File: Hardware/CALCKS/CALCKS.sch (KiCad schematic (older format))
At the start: 2 parts

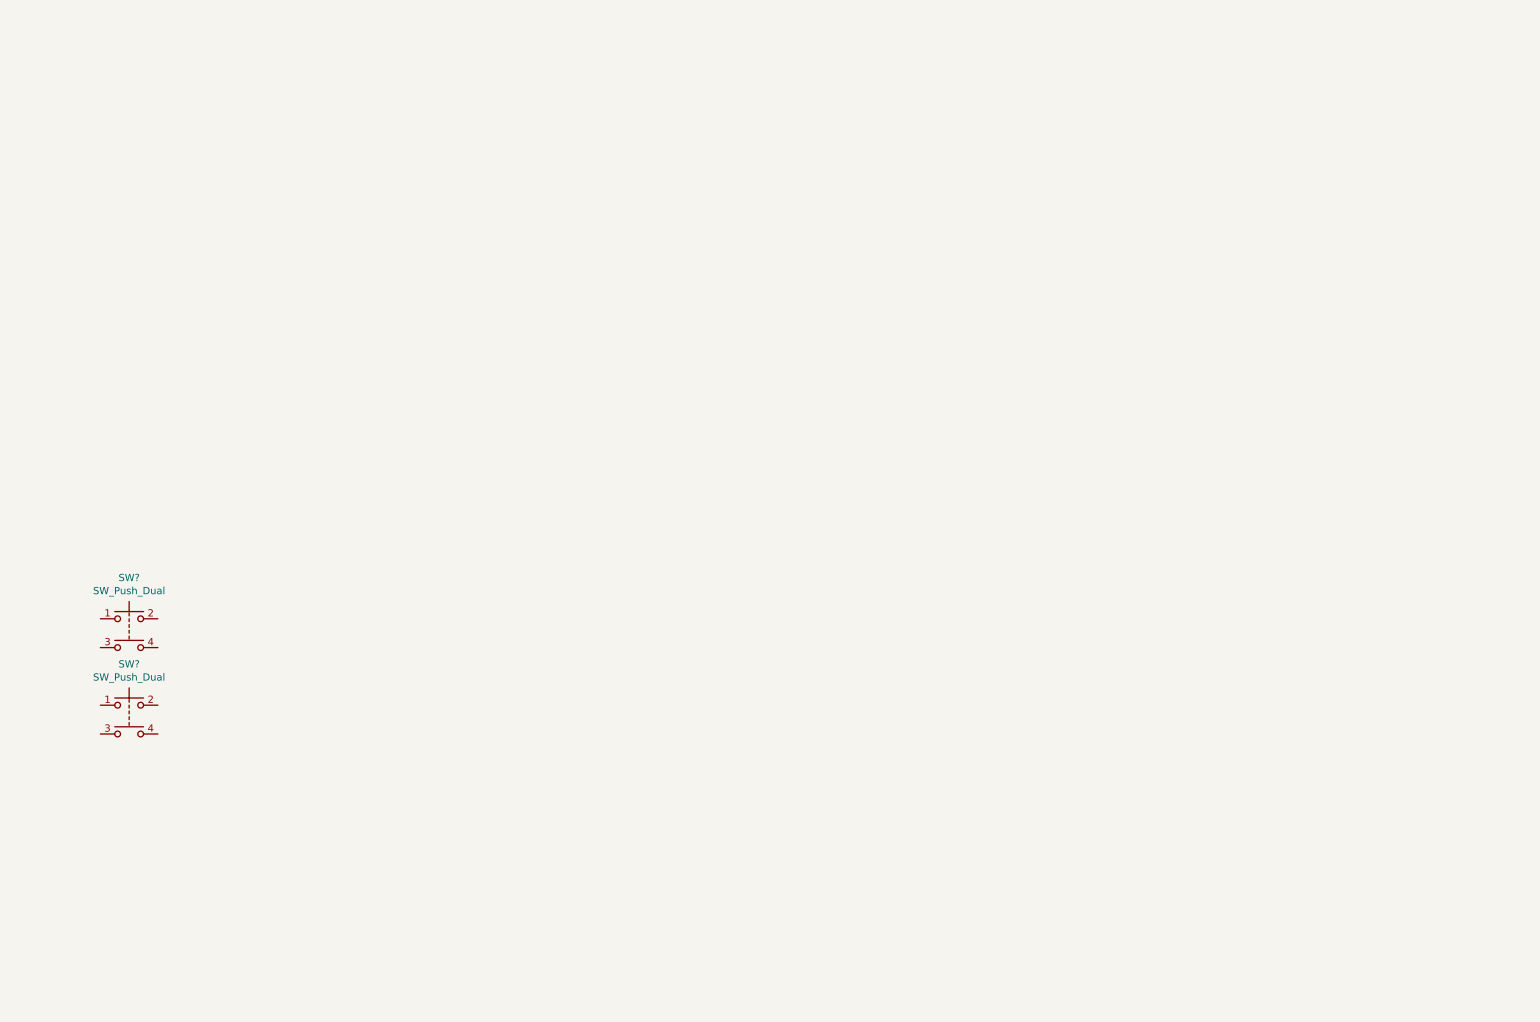
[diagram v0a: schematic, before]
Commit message: Add PCB progress from yesterday
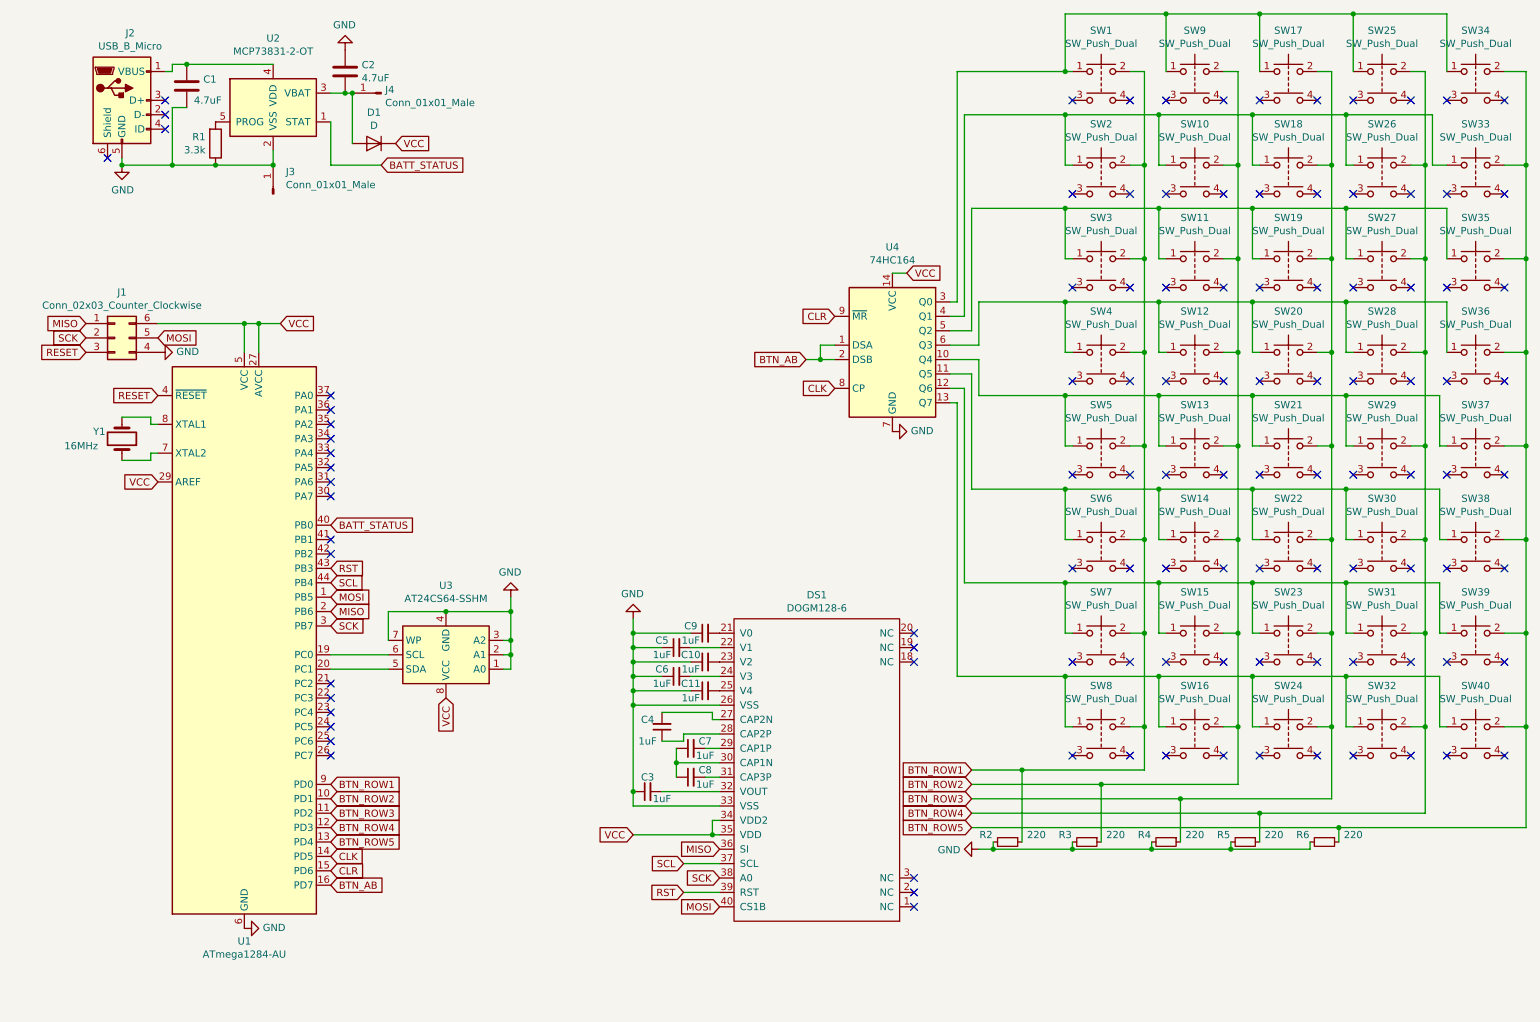
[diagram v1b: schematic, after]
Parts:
- removed SW? (x2): SW_Push_Dual, symbol Switch:SW_Push_Dual
- added C1, C2: 4.7uF, Capacitor_SMD:C_0805_2012Metric, symbol Device:C
- added C10, C11, C3, C4, C5, C6, C7, C8, C9: 1uF, Capacitor_SMD:C_0805_2012Metric, symbol Device:C_Small
- added D1: D, Diode_SMD:D_SOD-323, symbol Device:D
- added DS1: DOGM128-6, CALCKS:LCD_DOGM128-6, symbol Additional_Parts:DOGM128-6
- added J1: Conn_02x03_Counter_Clockwise, Connector_PinHeader_2.54mm:PinHeader_2x03_P2.54mm_Vertical, symbol Connector_Generic:Conn_02x03_Counter_Clockwise
- added J2: USB_B_Micro, Connector_USB:USB_Micro-B_Wuerth_629105150521, symbol Connector:USB_B_Micro
- added J3, J4: Conn_01x01_Male, TestPoint:TestPoint_Pad_D3.0mm, symbol Connector:Conn_01x01_Male
- added R1: 3.3k, Resistor_SMD:R_0805_2012Metric, symbol Device:R
- added R2, R3, R4, R5, R6: 220, Resistor_SMD:R_0805_2012Metric, symbol Device:R_Small
- added SW1, SW10, SW11, SW12, SW13, SW14, SW15, SW16, SW17, SW18, SW19, SW2, SW20, SW21, SW22, SW23, SW24, SW25, SW26, SW27, SW28, SW29, SW3, SW30, SW31, SW32, SW33, SW34, SW35, SW36, SW37, SW38, SW39, SW4, SW40, SW5, SW6, SW7, SW8, SW9: SW_Push_Dual, Downloaded Footprints:SW_TL3301SPF260QG, symbol Switch:SW_Push_Dual
- added U1: ATmega1284-AU, Package_QFP:TQFP-44_10x10mm_P0.8mm, symbol MCU_Microchip_ATmega:ATmega1284-AU
- added U2: MCP73831-2-OT, Package_TO_SOT_SMD:SOT-23-5, symbol Battery_Management:MCP73831-2-OT
- added U3: AT24CS64-SSHM, Package_SO:SOIC-8_3.9x4.9mm_P1.27mm, symbol Memory_EEPROM:AT24CS64-SSHM
- added U4: 74HC164, Package_SO:SOIC-14_3.9x8.7mm_P1.27mm, symbol 74xx:74HC164
- added Y1: 16MHz, Crystal:Crystal_SMD_HC49-SD, symbol Device:Crystal
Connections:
- new net: U1.19 (PC0), U3.6 (SCL)
- new net: U1.20 (PC1), U3.5 (SDA)
- new net: U1.7 (XTAL2), Y1.1
- new net: U1.8 (XTAL1), Y1.2
- new net: SW13.1, SW21.1, SW29.1, SW37.1, SW5.1, U4.10 (Q4)
- new net: SW14.1, SW22.1, SW30.1, SW38.1, SW6.1, U4.11 (Q5)
- new net: SW15.1, SW23.1, SW31.1, SW39.1, SW7.1, U4.12 (Q6)
- new net: SW16.1, SW24.1, SW32.1, SW40.1, SW8.1, U4.13 (Q7)
- new net: SW1.1, SW17.1, SW25.1, SW34.1, SW9.1, U4.3 (Q0)
- new net: SW10.1, SW18.1, SW2.1, SW26.1, SW33.1, U4.4 (Q1)
- new net: SW11.1, SW19.1, SW27.1, SW3.1, SW35.1, U4.5 (Q2)
- new net: SW12.1, SW20.1, SW28.1, SW36.1, SW4.1, U4.6 (Q3)
- new net: C2.2, D1.2 (A), J4.1 (Pin_1), U2.3 (VBAT)
- new net: C1.1, J2.1 (VBUS), U2.4 (VDD)
- new net: R1.2, U2.5 (PROG)
- new net: C9.2, DS1.21 (V0)
- new net: C5.2, DS1.22 (V1)
- new net: C10.2, DS1.23 (V2)
- new net: C6.2, DS1.24 (V3)
- new net: C11.2, DS1.25 (V4)
- new net: C4.2, DS1.27 (CAP2N)
- new net: C4.1, DS1.28 (CAP2P)
- new net: C7.2, DS1.29 (CAP1P)
- new net: C7.1, C8.1, DS1.30 (CAP1N)
- new net: C8.2, DS1.31 (CAP3P)
- new net: C3.2, DS1.32 (VOUT)
- new net BATT_STATUS: U1.40 (PB0), U2.1 (STAT)
- new net BTN_AB: U1.16 (PD7), U4.1 (DSA), U4.2 (DSB)
- new net BTN_ROW1: R2.1, SW1.2, SW2.2, SW3.2, SW4.2, SW5.2, SW6.2, SW7.2, SW8.2, U1.9 (PD0)
- new net BTN_ROW2: R3.1, SW10.2, SW11.2, SW12.2, SW13.2, SW14.2, SW15.2, SW16.2, SW9.2, U1.10 (PD1)
- new net BTN_ROW3: R4.1, SW17.2, SW18.2, SW19.2, SW20.2, SW21.2, SW22.2, SW23.2, SW24.2, U1.11 (PD2)
- new net BTN_ROW4: R5.1, SW25.2, SW26.2, SW27.2, SW28.2, SW29.2, SW30.2, SW31.2, SW32.2, U1.12 (PD3)
- new net BTN_ROW5: R6.1, SW33.2, SW34.2, SW35.2, SW36.2, SW37.2, SW38.2, SW39.2, SW40.2, U1.13 (PD4)
- new net CLK: U1.14 (PD5), U4.8 (CP)
- new net CLR: U1.15 (PD6), U4.9 (~MR)
- new net GND: C1.2, C10.1, C11.1, C2.1, C3.1, C5.1, C6.1, C9.1, DS1.26 (VSS), DS1.33 (VSS), J1.4 (Pin_4), J2.5 (GND), J3.1 (Pin_1), R1.1, R2.2, R3.2, R4.2, R5.2, R6.2, U1.18 (GND), U1.28 (GND), U1.39 (GND), U1.6 (GND), U2.2 (VSS), U3.1 (A0), U3.2 (A1), U3.3 (A2), U3.4 (GND), U3.7 (WP), U4.7 (GND)
- new net MISO: DS1.36 (SI), J1.1 (Pin_1), U1.2 (PB6)
- new net MOSI: DS1.40 (CS1B), J1.5 (Pin_5), U1.1 (PB5)
- new net RESET: J1.3 (Pin_3), U1.4 (~RESET)
- new net RST: DS1.39 (RST), U1.43 (PB3)
- new net SCK: DS1.38 (A0), J1.2 (Pin_2), U1.3 (PB7)
- new net SCL: DS1.37 (SCL), U1.44 (PB4)
- new net VCC: D1.1 (K), DS1.34 (VDD2), DS1.35 (VDD), J1.6 (Pin_6), U1.17 (VCC), U1.27 (AVCC), U1.29 (AREF), U1.38 (VCC), U1.5 (VCC), U3.8 (VCC), U4.14 (VCC)
- no-connect marks 0 -> 106

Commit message: Re-add version 2 of Hardware
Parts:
- added C1, C2: 30pF, Capacitor_SMD:C_0805_2012Metric, symbol Device:C
- added C17, C3, C5, C7: 0.1uF, Capacitor_SMD:C_0805_2012Metric, symbol Device:C
- added H1, H2, H3, H4, H5: MountingHole_Pad, MountingHole:MountingHole_2.2mm_M2_Pad_Via, symbol Mechanical:MountingHole_Pad
- added J5: Conn_01x04_Male, Connector_PinHeader_2.54mm:PinHeader_1x04_P2.54mm_Horizontal, symbol Connector:Conn_01x04_Male
- D1: footprint Diode_SMD:D_SOD-323 -> Diode_SMD:D_SOD-323_HandSoldering
- J3, J4: footprint TestPoint:TestPoint_Pad_D3.0mm -> Connector_Wire:SolderWirePad_1x01_Drill1.2mm
- Y1: value 16MHz -> 8MHz
- renumbered C5 to C10, C6 to C11, C7 to C12, C8 to C13, C9 to C14, C10 to C15, C11 to C16, C1 to C4, C2 to C6, C3 to C8, C4 to C9, J2 to J1, J1 to J2, R2 to R3, R3 to R4, R4 to R5, R5 to R6, R6 to R7, SW8 to SW1, SW5 to SW10, SW6 to SW11, SW7 to SW12, SW9 to SW13, SW10 to SW14, SW11 to SW15, SW12 to SW16, SW13 to SW17, SW14 to SW18, SW15 to SW19, SW16 to SW2, SW17 to SW20, SW18 to SW21, SW19 to SW22, SW20 to SW23, SW21 to SW24, SW22 to SW25, SW23 to SW26, SW25 to SW27, SW26 to SW28, SW27 to SW29, SW24 to SW3, SW28 to SW30, SW29 to SW31, SW30 to SW32, SW31 to SW33, SW33 to SW35, SW35 to SW36, SW36 to SW37, SW37 to SW38, SW38 to SW39, SW32 to SW4, SW39 to SW40, SW40 to SW5, SW1 to SW6, SW2 to SW7, SW3 to SW8, SW4 to SW9
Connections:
- net BTN_ROW1: now also SW10.4, SW11.4, SW12.4, SW6.4, SW7.4, SW8.4, SW9.4, U1.11 (PD2); no longer SW1.2, SW10.2, SW11.2, SW12.2, SW6.2, SW7.2, SW8.2, SW9.2, U1.9 (PD0)
- net BTN_ROW2: now also SW13.4, SW14.4, SW15.4, SW16.4, SW17.4, SW18.4, SW19.4, U1.12 (PD3); no longer SW13.2, SW14.2, SW15.2, SW16.2, SW17.2, SW18.2, SW19.2, SW2.2, U1.10 (PD1)
- net BTN_ROW3: now also SW20.4, SW21.4, SW22.4, SW23.4, SW24.4, SW25.4, SW26.4, U1.13 (PD4); no longer SW20.2, SW21.2, SW22.2, SW23.2, SW24.2, SW25.2, SW26.2, SW3.2, U1.11 (PD2)
- net BTN_ROW4: now also SW27.4, SW28.4, SW29.4, SW30.4, SW31.4, SW32.4, SW33.4, U1.14 (PD5); no longer SW27.2, SW28.2, SW29.2, SW30.2, SW31.2, SW32.2, SW33.2, SW4.2, U1.12 (PD3)
- net BTN_ROW5: now also SW34.4, SW35.4, SW36.4, SW37.4, SW38.4, SW39.4, SW40.4, U1.15 (PD6); no longer SW34.2, SW35.2, SW36.2, SW37.2, SW38.2, SW39.2, SW40.2, SW5.2, U1.13 (PD4)
- net CLK: now also U1.41 (PB1); no longer U1.14 (PD5)
- net CLR: now also U1.42 (PB2); no longer U1.15 (PD6)
- net VCC: now also C17.2, C5.2, C7.2, J5.4 (Pin_4); no longer U1.29 (AREF)
- net at U1.21 (PC2): now also SW1.1
- net at U1.22 (PC3): now also SW2.1
- net at U1.23 (PC4): now also SW3.1
- net at U1.24 (PC5): now also SW4.1
- net at U1.25 (PC6): now also SW5.1
- net at U1.7 (XTAL2), Y1.1: now also C2.2
- net at U1.8 (XTAL1), Y1.2: now also C1.1
- net -BATT: now reaches SW1.4
- net -BATT: now also C10.1, C11.1, C14.1, C15.1, C16.1, C6.1, C8.1, DS1.26 (VSS), DS1.33 (VSS), J2.4 (Pin_4), J3.1 (Pin_1), R3.2, R4.2, R5.2, R6.2, R7.2, SW2.4, SW3.4, SW4.4, SW5.4, U1.18 (GND), U1.28 (GND), U1.39 (GND), U1.6 (GND), U3.1 (A0), U3.2 (A1), U3.3 (A2), U3.4 (GND), U3.7 (WP), U4.7 (GND), C1.2, C17.1, C2.1, C3.1, C5.1, C7.1, H1.1, H2.1, H3.1, H4.1, H5.1, J5.1 (Pin_1)
- net +BATT: now reaches C6.2, D1.2 (A), J4.1 (Pin_1), U2.3 (VBAT)
- removed net GND: C10.1, C11.1, C14.1, C15.1, C16.1, C4.2, C6.1, C8.1, DS1.26 (VSS), DS1.33 (VSS), J1.5 (GND), J2.4 (Pin_4), J3.1 (Pin_1), R1.1, R3.2, R4.2, R5.2, R6.2, R7.2, U1.18 (GND), U1.28 (GND), U1.39 (GND), U1.6 (GND), U2.2 (VSS), U3.1 (A0), U3.2 (A1), U3.3 (A2), U3.4 (GND), U3.7 (WP), U4.7 (GND)
- new net: C3.2, U1.29 (AREF)
- new net: C4.2, J1.5 (GND), R1.1, U2.2 (VSS)
- new net RXD0: J5.3 (Pin_3), U1.9 (PD0)
- new net TXD0: J5.2 (Pin_2), U1.10 (PD1)
- now unconnected: U4.13 (Q7)
- no-connect marks 106 -> 100
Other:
- note added: "Current regulation:\n3.3k -> 303mA"
- moved on the sheet: D1, J1, R3, R4, R5, R6, R7, SW1, SW2, SW3, SW4, SW5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
